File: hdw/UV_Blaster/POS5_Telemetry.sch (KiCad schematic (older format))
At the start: 11 parts

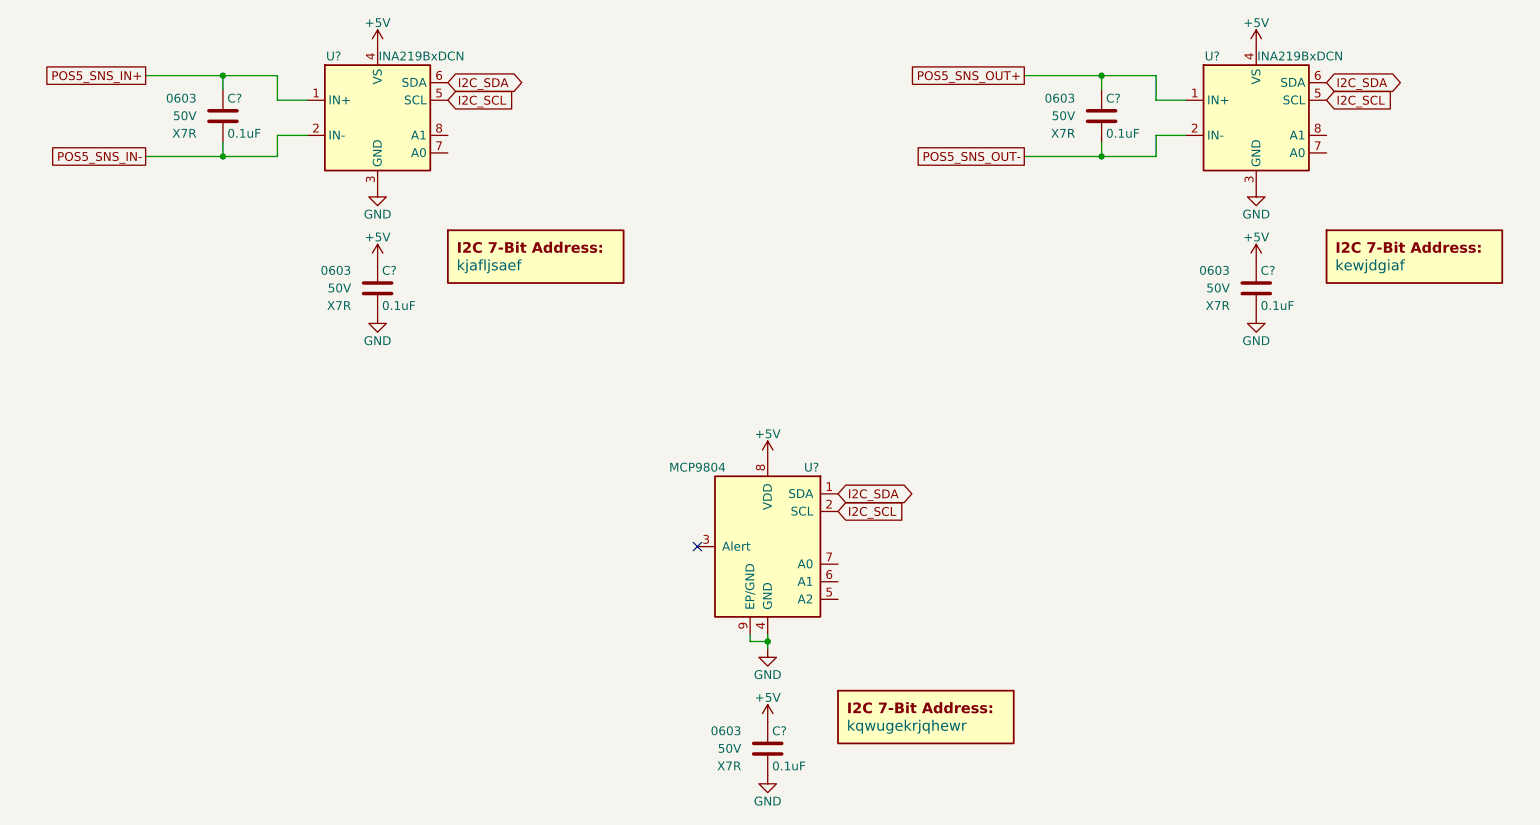
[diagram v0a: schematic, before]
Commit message: More sch work, netlist, part numbers, footprints
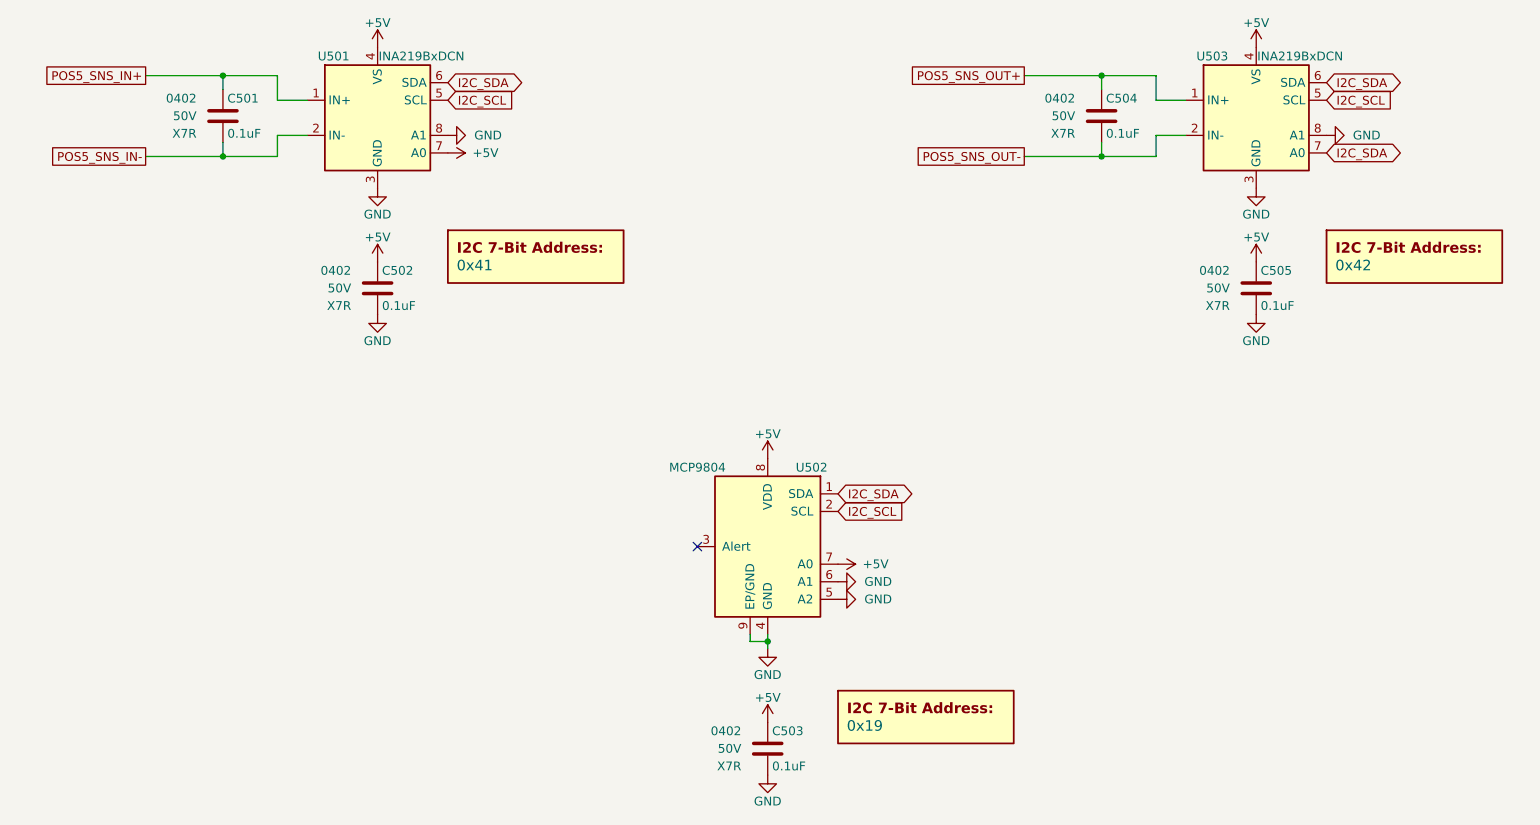
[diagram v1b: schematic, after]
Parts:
- removed DOC?: kjafljsaef, symbol Custom_Library:I2C_Address
- removed DOC?: kqwugekrjqhewr, symbol Custom_Library:I2C_Address
- removed DOC?: kewjdgiaf, symbol Custom_Library:I2C_Address
- added DOC501: 0x41, symbol Custom_Library:I2C_Address
- added DOC502: 0x19, symbol Custom_Library:I2C_Address
- added DOC503: 0x42, symbol Custom_Library:I2C_Address
- C501, C502, C503, C504, C505: renamed from C?; footprint Capacitors_SMD:C_0603 -> Capacitors_SMD:C_0402; Configuration (none) -> Telemetry; Digi-Key PN 399-6856-1-ND -> 490-10701-1-ND; display_footprint 0603 -> 0402
- U501, U502, U503: renamed from U?; Configuration (none) -> Telemetry
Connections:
- net +5V: now also U501.7 (A0), U502.7 (A0)
- net GND: now also U501.8 (A1), U502.5 (A2), U502.6 (A1), U503.8 (A1)
- net I2C_SDA: now also U503.7 (A0)
